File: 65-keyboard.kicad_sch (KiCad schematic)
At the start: 20 parts, among them SW1 SW_Push, U1 ATmega32U4-A, Y1 Crystal_GND24_Small

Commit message: more routing
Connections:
- net COL5: now also U1.36 (PF7); no longer U1.37 (PF6)
- net COL6: now also U1.37 (PF6); no longer U1.36 (PF7)
- net ROW1: now also U1.39 (PF4); no longer U1.38 (PF5)
- net ROW2: now also U1.40 (PF1); no longer U1.41 (PF0)
- net ROW3: now also U1.41 (PF0); no longer U1.40 (PF1)
- net ROW4: now also U1.38 (PF5); no longer U1.39 (PF4)
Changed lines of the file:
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@@
     )
   )
-  (global_label "ROW4" (shape input) (at 70.358 96.52 0) (fields_autoplaced)
+  (global_label "ROW4" (shape input) (at 70.358 99.06 0) (fields_autoplaced)
     (effects (font (size 1.27 1.27)) (justify left))
-    (property "Intersheet References" "${INTERSHEET_REFS}" (id 0) (at 78.0325 96.4406 0)
+    (property "Intersheet References" "${INTERSHEET_REFS}" (id 0) (at 78.0325 98.9806 0)
       (effects (font (size 1.27 1.27)) (justify left) hide)
     )
   )
-  (global_label "COL5" (shape input) (at 70.358 101.6 0) (fields_autoplaced)
+  (global_label "COL5" (shape input) (at 70.358 104.14 0) (fields_autoplaced)
     (effects (font (size 1.27 1.27)) (justify left))
-    (property "Intersheet References" "${INTERSHEET_REFS}" (id 0) (at 77.6092 101.5206 0)
+    (property "Intersheet References" "${INTERSHEET_REFS}" (id 0) (at 77.6092 104.0606 0)
       (effects (font (size 1.27 1.27)) (justify left) hide)
     )
@@
     )
   )
-  (global_label "ROW3" (shape input) (at 70.358 93.98 0) (fields_autoplaced)
+  (global_label "ROW3" (shape input) (at 70.358 91.44 0) (fields_autoplaced)
     (effects (font (size 1.27 1.27)) (justify left))
-    (property "Intersheet References" "${INTERSHEET_REFS}" (id 0) (at 78.0325 93.9006 0)
+    (property "Intersheet References" "${INTERSHEET_REFS}" (id 0) (at 78.0325 91.3606 0)
       (effects (font (size 1.27 1.27)) (justify left) hide)
     )
@@
     )
   )
-  (global_label "COL6" (shape input) (at 70.358 104.14 0) (fields_autoplaced)
+  (global_label "COL6" (shape input) (at 70.358 101.6 0) (fields_autoplaced)
     (effects (font (size 1.27 1.27)) (justify left))
-    (property "Intersheet References" "${INTERSHEET_REFS}" (id 0) (at 77.6092 104.0606 0)
+    (property "Intersheet References" "${INTERSHEET_REFS}" (id 0) (at 77.6092 101.5206 0)
       (effects (font (size 1.27 1.27)) (justify left) hide)
     )
@@
     )
   )
-  (global_label "ROW1" (shape input) (at 70.358 99.06 0) (fields_autoplaced)
+  (global_label "ROW1" (shape input) (at 70.358 96.52 0) (fields_autoplaced)
     (effects (font (size 1.27 1.27)) (justify left))
-    (property "Intersheet References" "${INTERSHEET_REFS}" (id 0) (at 78.0325 98.9806 0)
+    (property "Intersheet References" "${INTERSHEET_REFS}" (id 0) (at 78.0325 96.4406 0)
       (effects (font (size 1.27 1.27)) (justify left) hide)
     )
@@
     )
   )
-  (global_label "ROW2" (shape input) (at 70.358 91.44 0) (fields_autoplaced)
+  (global_label "ROW2" (shape input) (at 70.358 93.98 0) (fields_autoplaced)
     (effects (font (size 1.27 1.27)) (justify left))
-    (property "Intersheet References" "${INTERSHEET_REFS}" (id 0) (at 78.0325 91.3606 0)
+    (property "Intersheet References" "${INTERSHEET_REFS}" (id 0) (at 78.0325 93.9006 0)
       (effects (font (size 1.27 1.27)) (justify left) hide)
     )

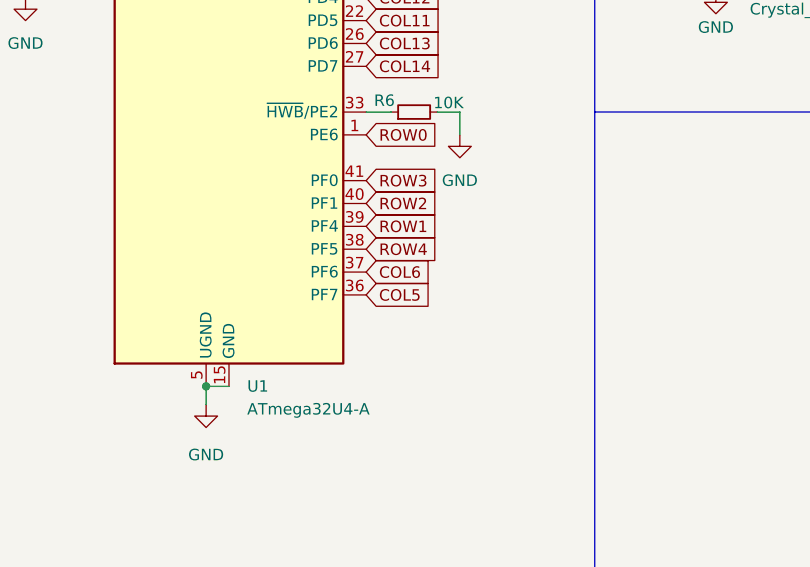
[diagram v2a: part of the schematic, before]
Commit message: rerouted pcb
fixing drc issues
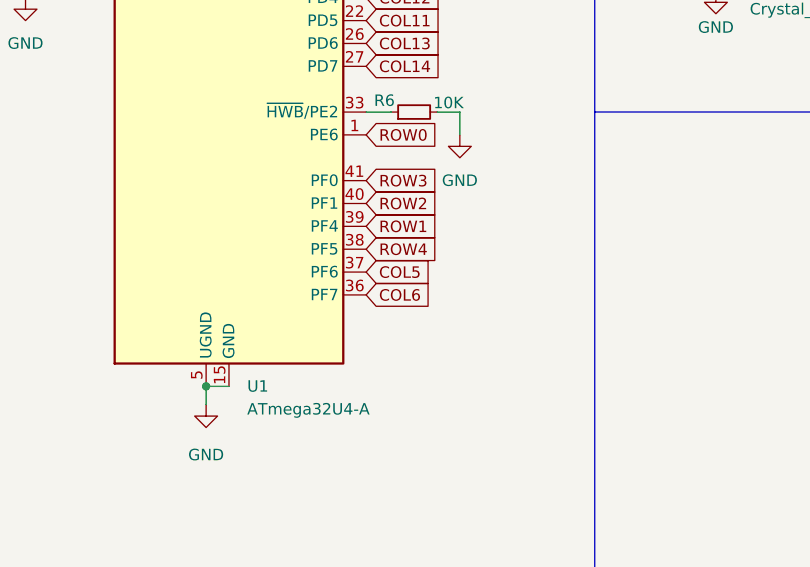
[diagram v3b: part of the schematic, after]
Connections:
- net COL5: now also U1.37 (PF6); no longer U1.36 (PF7)
- net COL6: now also U1.36 (PF7); no longer U1.37 (PF6)
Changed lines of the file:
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@@
     )
   )
-  (global_label "COL5" (shape input) (at 70.358 104.14 0) (fields_autoplaced)
+  (global_label "COL5" (shape input) (at 70.358 101.6 0) (fields_autoplaced)
     (effects (font (size 1.27 1.27)) (justify left))
-    (property "Intersheet References" "${INTERSHEET_REFS}" (id 0) (at 77.6092 104.0606 0)
+    (property "Intersheet References" "${INTERSHEET_REFS}" (id 0) (at 77.6092 101.5206 0)
       (effects (font (size 1.27 1.27)) (justify left) hide)
     )
@@
     )
   )
-  (global_label "COL6" (shape input) (at 70.358 101.6 0) (fields_autoplaced)
+  (global_label "COL6" (shape input) (at 70.358 104.14 0) (fields_autoplaced)
     (effects (font (size 1.27 1.27)) (justify left))
-    (property "Intersheet References" "${INTERSHEET_REFS}" (id 0) (at 77.6092 101.5206 0)
+    (property "Intersheet References" "${INTERSHEET_REFS}" (id 0) (at 77.6092 104.0606 0)
       (effects (font (size 1.27 1.27)) (justify left) hide)
     )
